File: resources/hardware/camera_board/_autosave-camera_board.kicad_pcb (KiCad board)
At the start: 2 copper layers, 95.2 x 56.2 mm, 12 parts, among them P1 CONN_01X03, Q1 Q_NPN_EBC

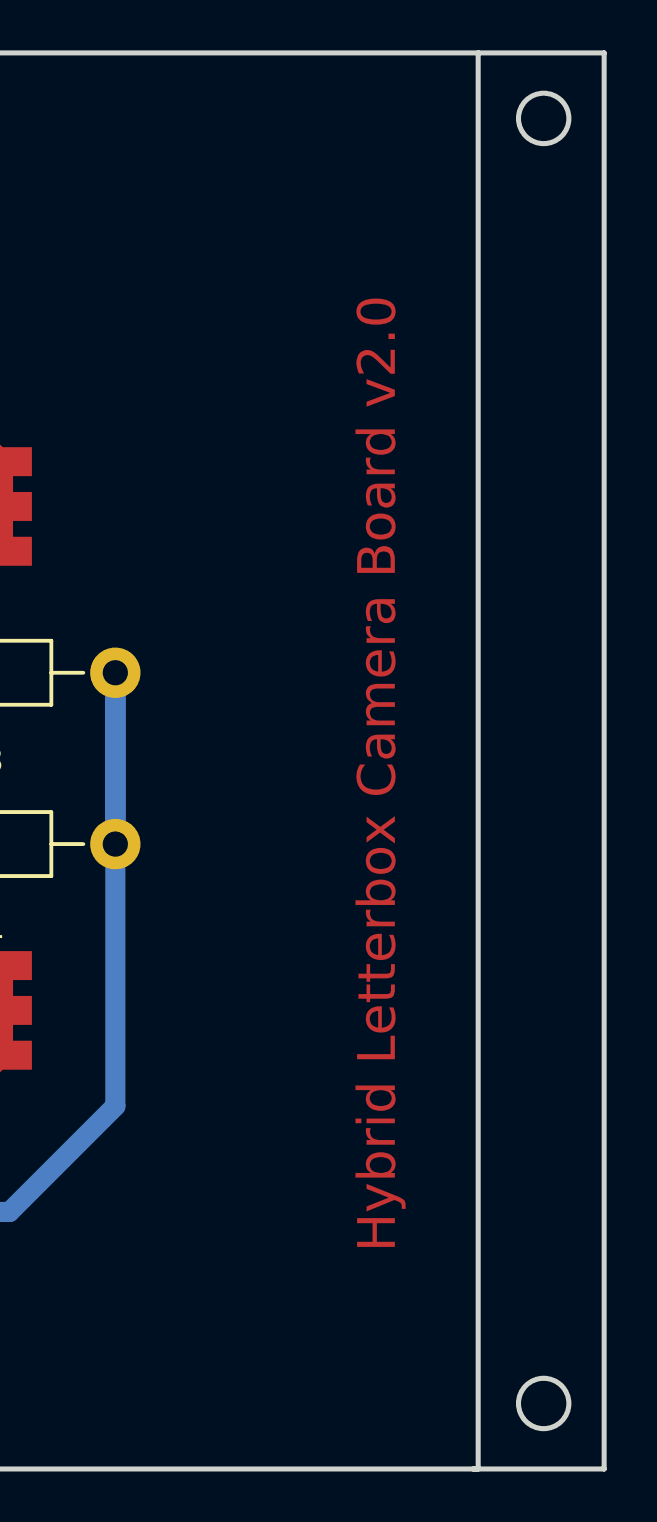
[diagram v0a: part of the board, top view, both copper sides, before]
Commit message: wrote threshold, extractRegion and findMarker for cardScanner class
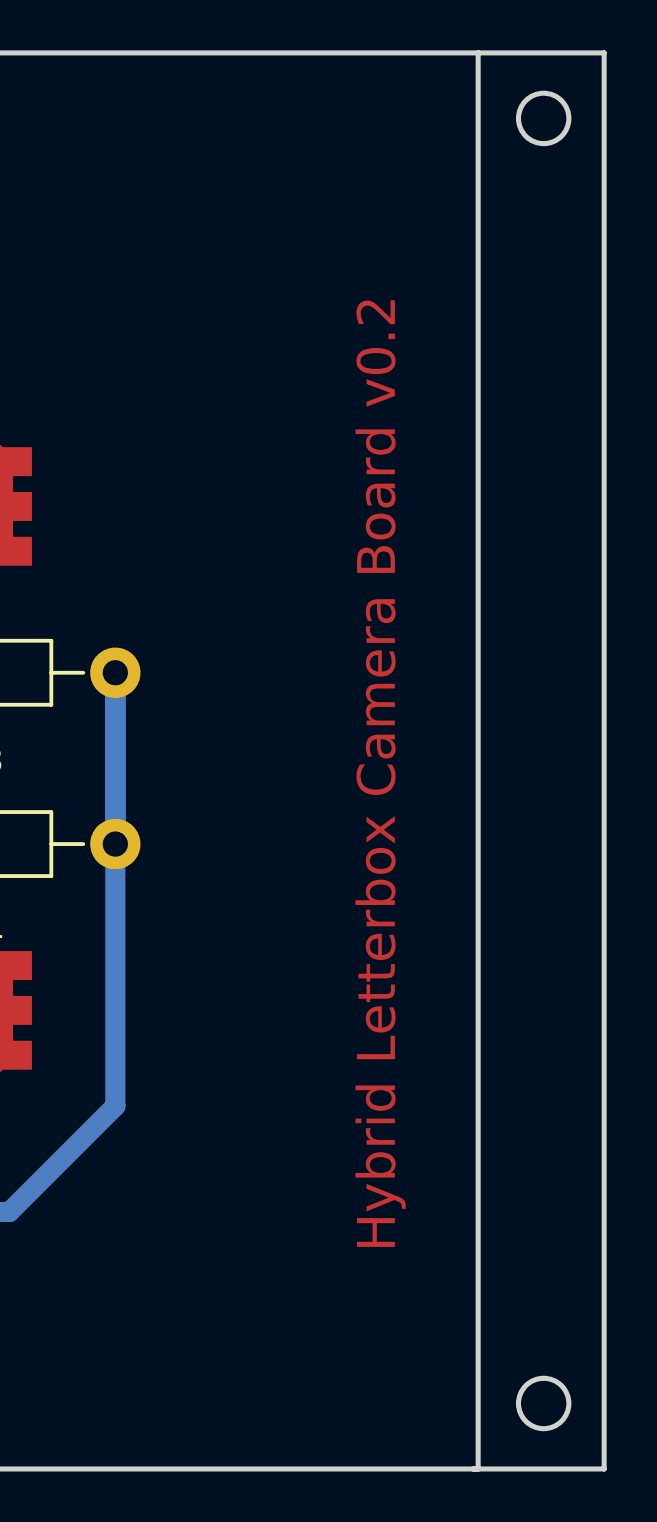
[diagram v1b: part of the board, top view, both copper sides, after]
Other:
- board text added: "Hybrid Letterbox Camera Board v0.2"
- board text removed: "Hybrid Letterbox Camera Board v2.0"
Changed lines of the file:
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@@
     (links 31)
     (no_connects 1)
-    (area 87.899999 60.099999 183.300001 116.500001)
+    (area 87.899999 59.514624 183.300001 117.265881)
     (thickness 1.6)
     (drawings 49)
@@
       (outputformat 4)
       (mirror false)
-      (drillshape 0)
+      (drillshape 1)
       (scaleselection 1)
       (outputdirectory plots/))
@@
     (effects (font (size 1.5 1.5) (thickness 0.3)))
   )
-  (gr_text "Hybrid Letterbox Camera Board v2.0" (at 174.2 88.8 90) (layer F.Cu)
+  (gr_text "Hybrid Letterbox Camera Board v0.2\n" (at 174.2 88.8 90) (layer F.Cu)
     (effects (font (size 1.5 1.5) (thickness 0.3)))
   )
